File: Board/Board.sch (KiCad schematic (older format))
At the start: 42 parts

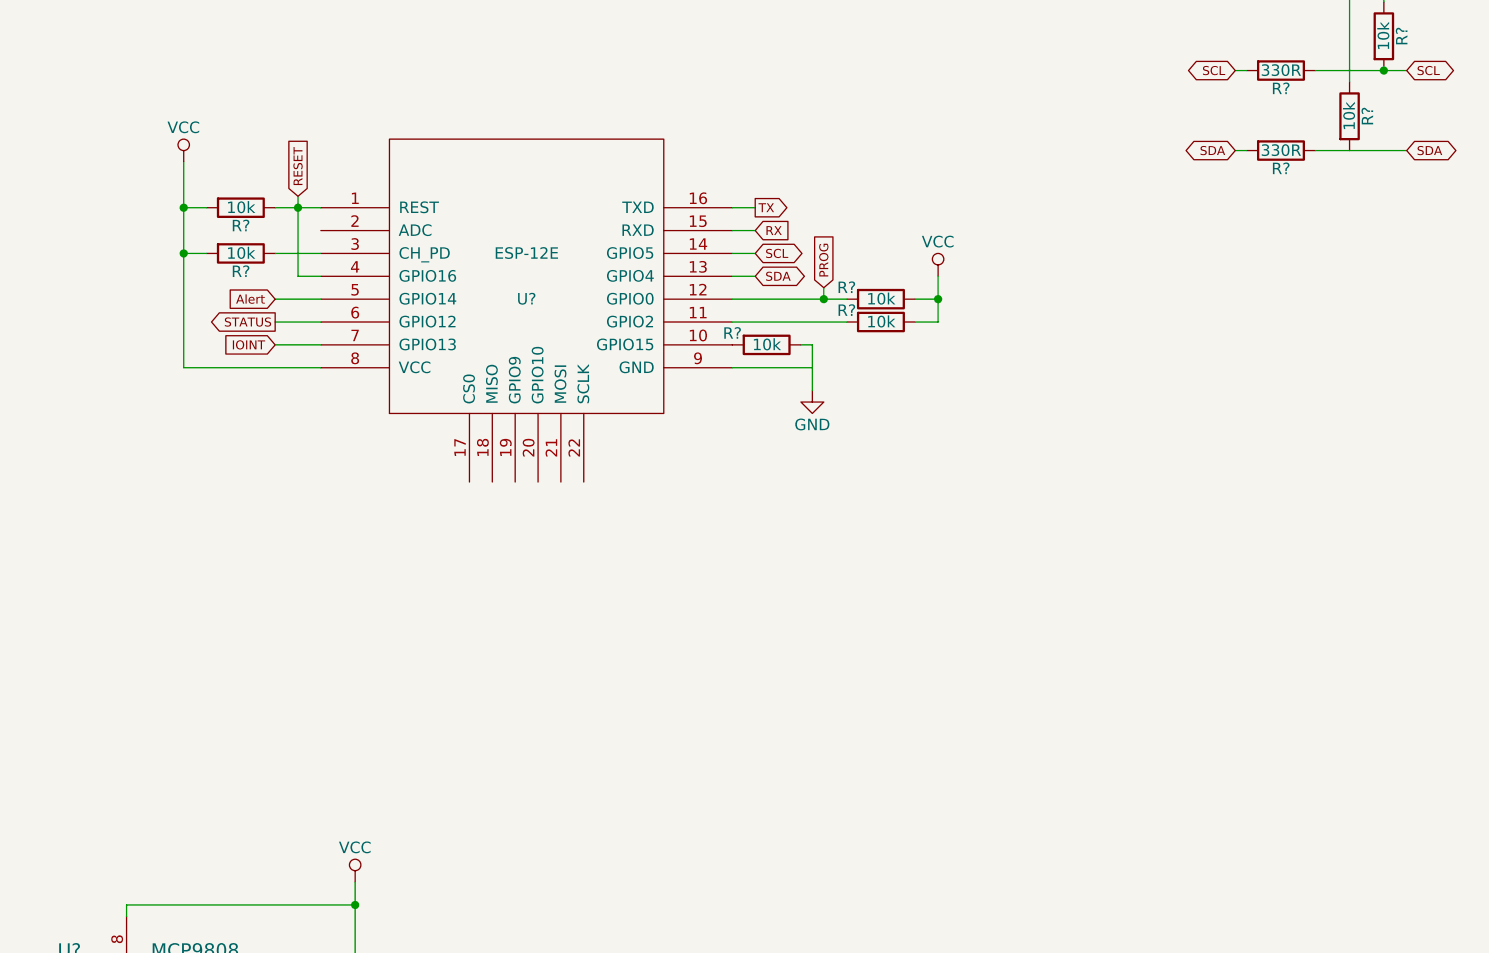
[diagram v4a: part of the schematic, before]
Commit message: WS2812 for status and bypass for ESP
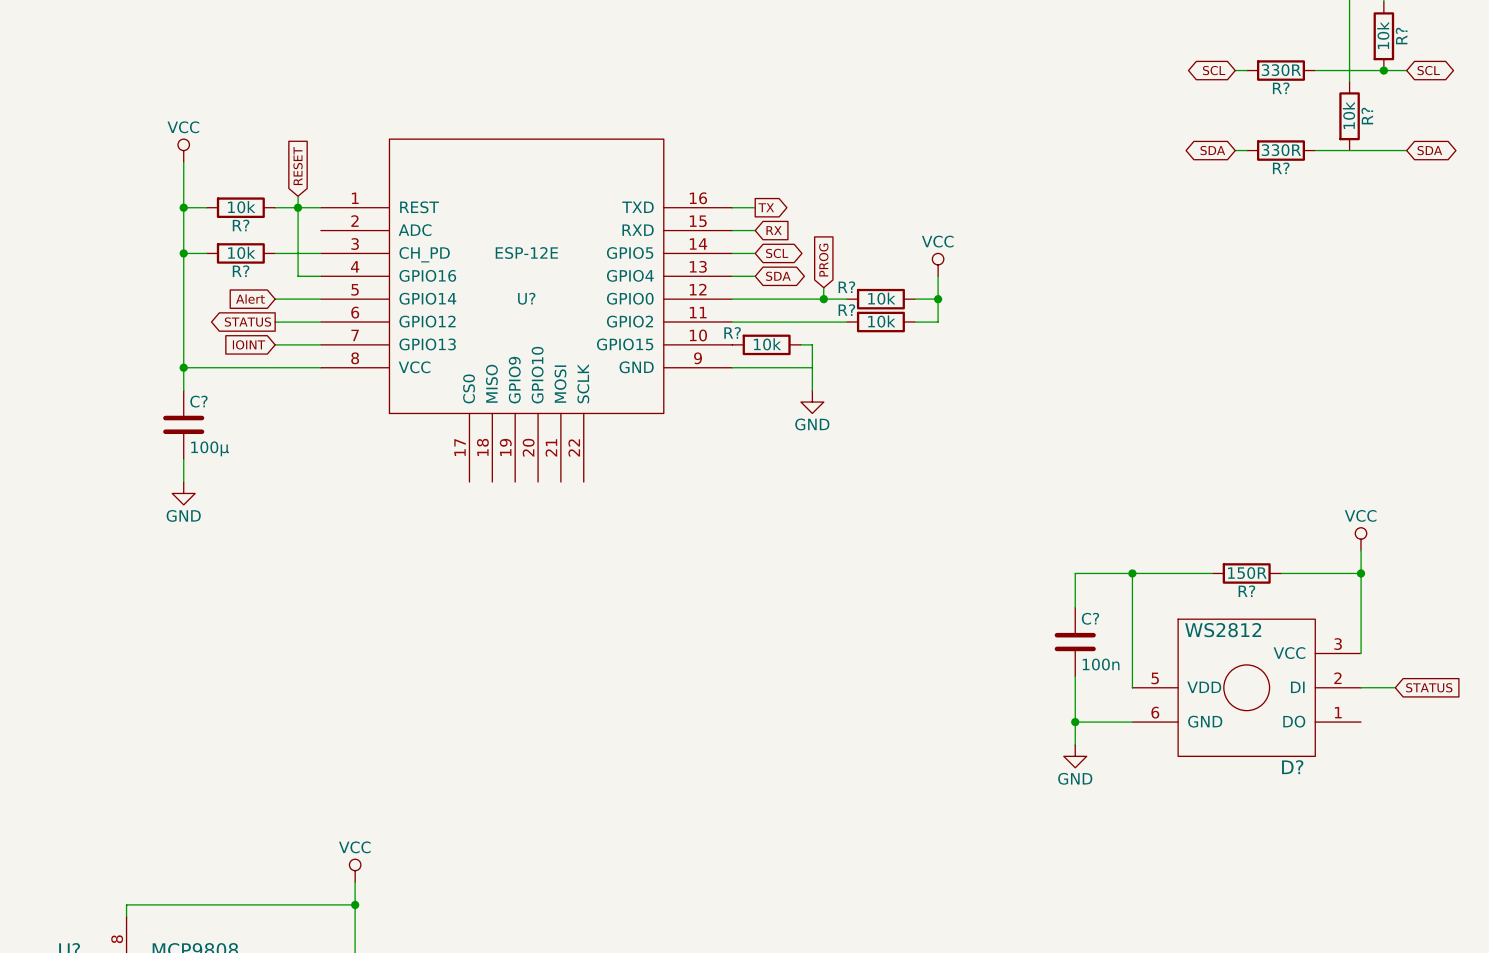
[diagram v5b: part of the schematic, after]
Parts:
- added C?: 100n, Capacitors_SMD:C_0603_HandSoldering, symbol C
- added C?: 100µ, symbol C
- added D?: WS2812, LEDs:LED_WS2812-PLCC6, symbol WS2812
- added R?: 150R, Resistors_SMD:R_0603_HandSoldering, symbol R
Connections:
- net GND: now also C?.2, C?.2, D?.6 (GND)
- net STATUS: now also D?.2 (DI)
- net VCC: now also C?.1, D?.3 (VCC), R?.1
- new net: C?.1, D?.5 (VDD), R?.2
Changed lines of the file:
@@
 Connection ~ 4200 1000
 Wire Wire Line
-	5400 2850 5400 3750
+	5400 2850 5400 3850
 Connection ~ 5400 3250
 Text GLabel 8200 3400 1    39   Input ~ 0
@@
 Wire Wire Line
 	5800 3650 6000 3650
+$Comp
+L R R?
+U 1 1 5AD4F33A
+P 10050 4650
+F 0 "R?" V 10130 4650 50  0000 C CNN
+F 1 "150R" V 10050 4650 50  0000 C CNN
+F 2 "Resistors_SMD:R_0603_HandSoldering" V 9980 4650 50  0001 C CNN
+F 3 "" H 10050 4650 50  0000 C CNN
+	1    10050 4650
+	0    1    1    0
+$EndComp
+Wire Wire Line
+	10550 4550 10550 5000
+Wire Wire Line
+	10550 4650 10200 4650
+Wire Wire Line
+	9300 4650 9900 4650
+Wire Wire Line
+	9550 4650 9550 5150
+$Comp
+L VCC #PWR?
+U 1 1 5AD4F68E
+P 10550 4550
+F 0 "#PWR?" H 10550 4400 50  0001 C CNN
+F 1 "VCC" H 10550 4700 50  0000 C CNN
+F 2 "" H 10550 4550 50  0000 C CNN
+F 3 "" H 10550 4550 50  0000 C CNN
+	1    10550 4550
+	1    0    0    -1
+$EndComp
+Connection ~ 10550 4650
+$Comp
+L C C?
+U 1 1 5AD4F92C
+P 9300 4950
+F 0 "C?" H 9325 5050 50  0000 L CNN
+F 1 "100n" H 9325 4850 50  0000 L CNN
+F 2 "Capacitors_SMD:C_0603_HandSoldering" H 9338 4800 50  0001 C CNN
+F 3 "" H 9300 4950 50  0000 C CNN
+	1    9300 4950
+	1    0    0    -1
+$EndComp
+Wire Wire Line
+	9300 4800 9300 4650
+Connection ~ 9550 4650
+Wire Wire Line
+	9300 5100 9300 5400
+Wire Wire Line
+	9300 5300 9550 5300
+$Comp
+L GND #PWR?
+U 1 1 5AD4FEAF
+P 9300 5400
+F 0 "#PWR?" H 9300 5150 50  0001 C CNN
+F 1 "GND" H 9300 5250 50  0000 C CNN
+F 2 "" H 9300 5400 50  0000 C CNN
+F 3 "" H 9300 5400 50  0000 C CNN
+	1    9300 5400
+	1    0    0    -1
+$EndComp
+Connection ~ 9300 5300
+Text GLabel 10700 5150 2    39   Input ~ 0
+STATUS
+Wire Wire Line
+	10700 5150 10550 5150
+$Comp
+L WS2812 D?
+U 1 1 5AD50C56
+P 10050 5150
+F 0 "D?" H 10250 4800 60  0000 C CNN
+F 1 "WS2812" H 9950 5400 60  0000 C CNN
+F 2 "LEDs:LED_WS2812-PLCC6" H 10100 4400 60  0001 C CNN
+F 3 "https://github.com/netz39/kicad_parts/raw/master/datasheets/WS2812.pdf" H 10300 4500 60  0001 C CNN
+	1    10050 5150
+	1    0    0    -1
+$EndComp
+$Comp
+L C C?
+U 1 1 5AD51B02
+P 5400 4000
+F 0 "C?" H 5425 4100 50  0000 L CNN
+F 1 "100µ" H 5425 3900 50  0000 L CNN
+F 2 "" H 5438 3850 50  0001 C CNN
+F 3 "" H 5400 4000 50  0000 C CNN
+	1    5400 4000
+	1    0    0    -1
+$EndComp
+$Comp
+L GND #PWR?
+U 1 1 5AD51CC2
+P 5400 4250
+F 0 "#PWR?" H 5400 4000 50  0001 C CNN
+F 1 "GND" H 5400 4100 50  0000 C CNN
+F 2 "" H 5400 4250 50  0000 C CNN
+F 3 "" H 5400 4250 50  0000 C CNN
+	1    5400 4250
+	1    0    0    -1
+$EndComp
+Connection ~ 5400 3750
+Wire Wire Line
+	5400 4150 5400 4250
 $EndSCHEMATC

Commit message: Footprints and TODOs
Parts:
- C? (x3): footprint (none) -> Capacitors_SMD:C_0603_HandSoldering
- D?: footprint (none) -> n39-kicad:VQE24
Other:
- note added: "Footprint"
- note added: "Prog Button"
- note added: "Reset Button"
- note added: "Value\n"
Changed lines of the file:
@@
 Sheet 1 1
 Title "Cloud Temperature Sensor"
-Date "2018-04-15"
+Date "2018-04-16"
 Rev ""
 Comp "penguineer"
@@
 F 0 "D?" H 2950 6050 60  0000 C CNN
 F 1 "VQE24" H 2300 6250 60  0000 C CNN
-F 2 "" H 2150 6550 60  0001 C CNN
+F 2 "n39-kicad:VQE24" H 2150 6550 60  0001 C CNN
 F 3 "https://github.com/netz39/kicad_parts/raw/master/datasheets/VQE_7segment.pdf" H 2500 5750 60  0001 C CNN
 	1    2300 6700
@@
 F 0 "C?" H 1425 4050 50  0000 L CNN
 F 1 "33p" H 1425 3850 50  0000 L CNN
-F 2 "" H 1438 3800 50  0001 C CNN
+F 2 "Capacitors_SMD:C_0603_HandSoldering" H 1438 3800 50  0001 C CNN
 F 3 "" H 1400 3950 50  0000 C CNN
 	1    1400 3950
@@
 F 0 "C?" H 1175 5050 50  0000 L CNN
 F 1 "100µ" H 1175 4850 50  0000 L CNN
-F 2 "" H 1188 4800 50  0001 C CNN
+F 2 "Capacitors_SMD:C_0603_HandSoldering" H 1188 4800 50  0001 C CNN
 F 3 "" H 1150 4950 50  0000 C CNN
 	1    1150 4950
@@
 F 0 "C?" H 5425 4100 50  0000 L CNN
 F 1 "100µ" H 5425 3900 50  0000 L CNN
-F 2 "" H 5438 3850 50  0001 C CNN
+F 2 "Capacitors_SMD:C_0603_HandSoldering" H 5438 3850 50  0001 C CNN
 F 3 "" H 5400 4000 50  0000 C CNN
 	1    5400 4000
@@
 Wire Wire Line
 	5400 4150 5400 4250
+Text Notes 2250 1650 0    60   ~ 0
+Footprint
+Text Notes 4400 1700 0    60   ~ 0
+Value\n
+Text Notes 5950 1550 0    60   ~ 0
+Reset Button
+Text Notes 5950 1650 0    60   ~ 0
+Prog Button
 $EndSCHEMATC

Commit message: Schematic: final TODOs
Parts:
- removed C?: 0.1µ, Capacitors_SMD:C_0603_HandSoldering, symbol C
- removed C?: 100µ, Capacitors_SMD:C_0603_HandSoldering, symbol C
- added C? (x3): 22µ, Capacitors_SMD:C_1206_HandSoldering, symbol C
- added C?: 100n, Capacitors_SMD:C_0603_HandSoldering, symbol C
- added R? (x2): 330R, Resistors_SMD:R_0603_HandSoldering, symbol R
- added R? (x2): 10k, Resistors_SMD:R_0603_HandSoldering, symbol R
- added SW? (x2): SW_SPST, symbol SW_SPST
- C?: value 100µ -> 100n
- C?: value 0.1µ -> 22µ; footprint Capacitors_SMD:C_0603_HandSoldering -> Capacitors_SMD:C_1206_HandSoldering
- C?: value 100µ -> 10µ; footprint (none) -> Capacitors_SMD:C_1206_HandSoldering
- D?: footprint LEDs:LED_0603 -> LEDs:LED_1206
- R?: value R -> 39R
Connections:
- net Alert: now also R?.1
- net GND: now also C?.2, C?.2, C?.2, C?.2, SW?.1 (A), SW?.1 (A)
- net IOINT: now also R?.1
- net PROG: now also R?.1
- net RESET: now also R?.1
- net VCC: now also C?.1, C?.1, C?.1, C?.1, R?.2, R?.2; no longer C?.1, U?.8 (VCC)
- new net: C?.1, U?.8 (VCC)
- new net: R?.2, SW?.2 (B) (x2)
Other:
- note removed: "Footprint"
- note removed: "Prog Button"
- note removed: "Reset Button"
- note removed: "Value\n"
- moved on the sheet: C?, D?, P?, R?, U?

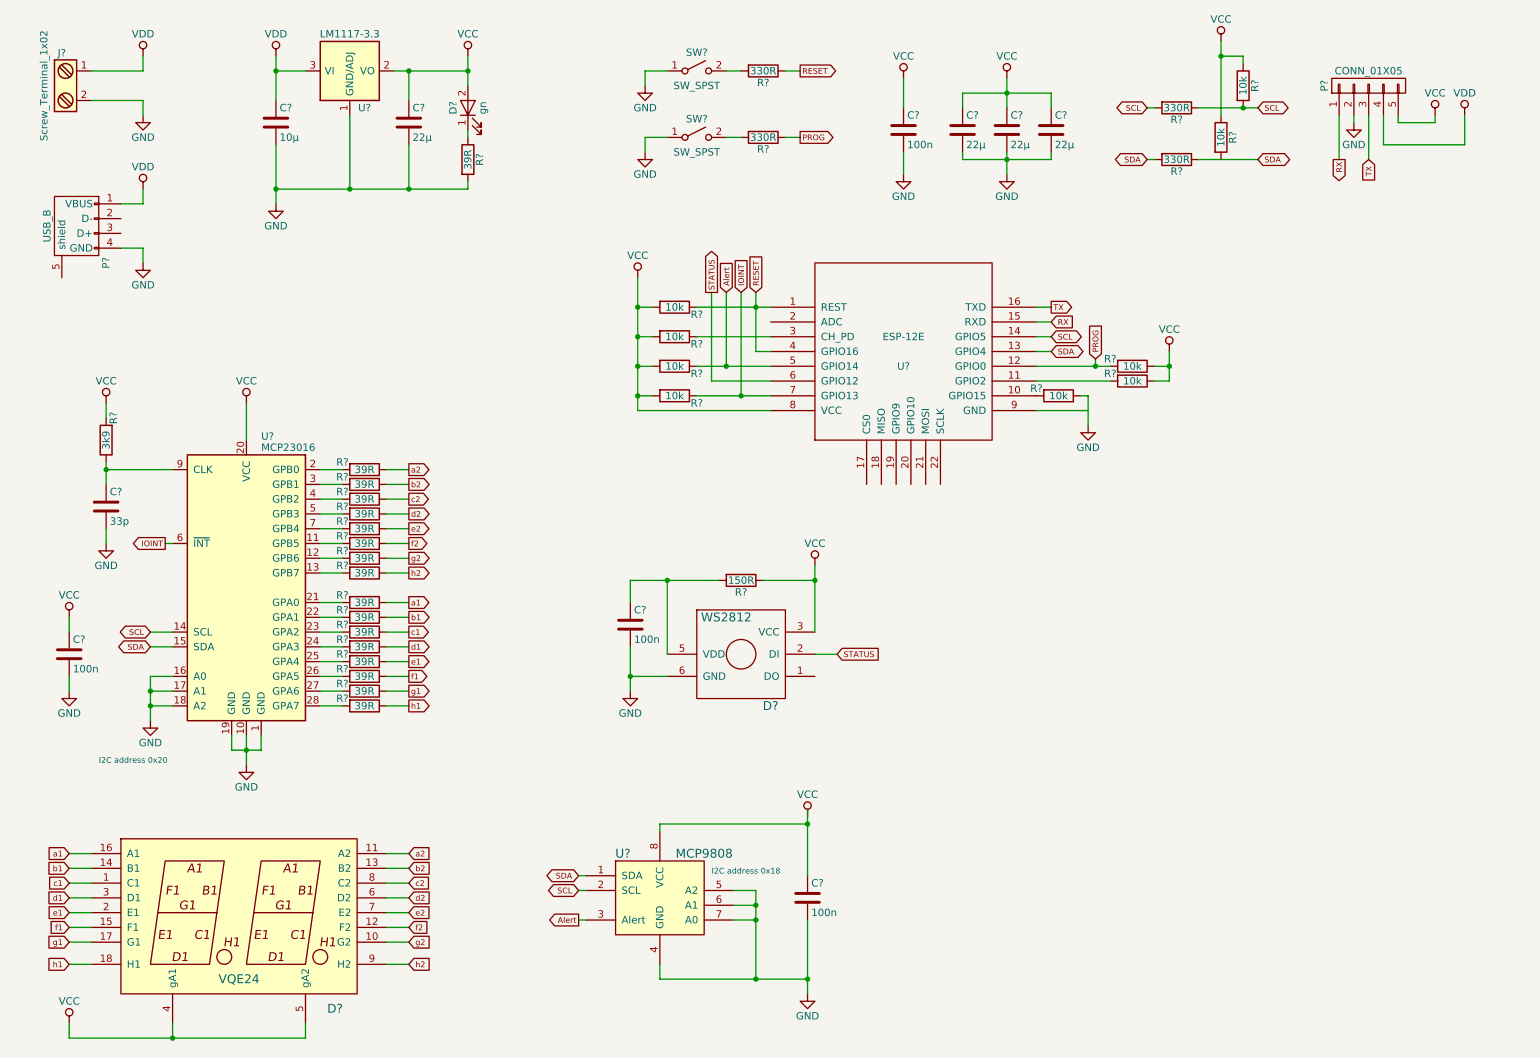
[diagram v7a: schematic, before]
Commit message: Schematic: Annotate symbols
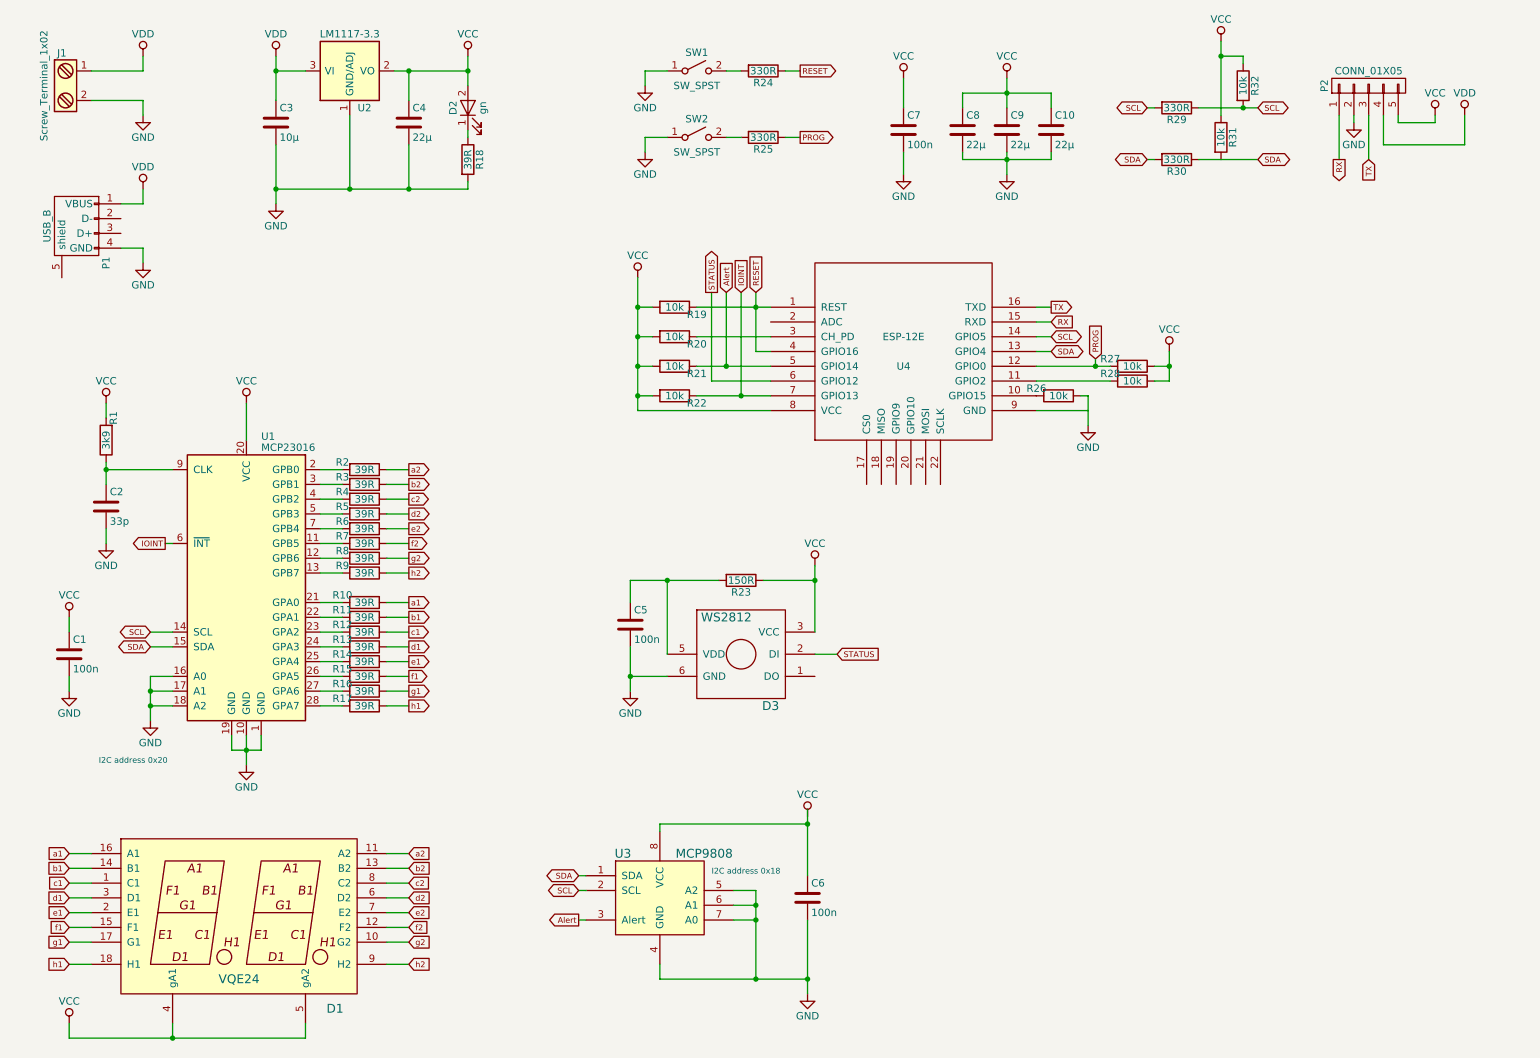
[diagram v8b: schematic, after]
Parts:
- gave numbers to parts that had none: 54
